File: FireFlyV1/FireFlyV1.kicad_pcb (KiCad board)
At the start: 2 copper layers, 2 parts, among them U1 RP2040, U2 W25Q32JVSS

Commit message: FireFlyV1 PCB begin
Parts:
- added C1: 15pF, Capacitor_SMD:C_0402_1005Metric, F.Cu at (149.2, 86.5)
- added C10: 0.1uF, Capacitor_SMD:C_0402_1005Metric, F.Cu at (152.1, 94.3)
- added C11: 1uF, Capacitor_SMD:C_0402_1005Metric, F.Cu at (155.0, 86.5)
- added C12: 1uF, Capacitor_SMD:C_0402_1005Metric, F.Cu at (155.0, 88.4)
- added C13: 100nF, Capacitor_SMD:C_0402_1005Metric, F.Cu at (155.0, 90.4)
- added C14: 100nF, Capacitor_SMD:C_0402_1005Metric, F.Cu at (155.0, 92.4)
- added C15: 100nF, Capacitor_SMD:C_0402_1005Metric, F.Cu at (155.0, 94.3)
- added C16: 100nF, Capacitor_SMD:C_0402_1005Metric, F.Cu at (157.9, 86.5)
- added C17: 100nF, Capacitor_SMD:C_0402_1005Metric, F.Cu at (157.9, 88.4)
- added C18: 100nF, Capacitor_SMD:C_0402_1005Metric, F.Cu at (157.9, 90.4)
- added C19: 100nF, Capacitor_SMD:C_0402_1005Metric, F.Cu at (157.9, 92.4)
- added C2: 15pF, Capacitor_SMD:C_0402_1005Metric, F.Cu at (149.2, 88.4)
- added C20: 1uF, Capacitor_SMD:C_0402_1005Metric, F.Cu at (157.9, 94.3)
- added C3: 10uF, Capacitor_SMD:C_0402_1005Metric, F.Cu at (149.2, 90.4)
- added C4: 10uF, Capacitor_SMD:C_0402_1005Metric, F.Cu at (149.2, 92.4)
- added C5: 10uF, Capacitor_SMD:C_0402_1005Metric, F.Cu at (149.2, 94.3)
- added C6: 2.2uF, Capacitor_SMD:C_0402_1005Metric, F.Cu at (152.1, 86.5)
- added C7: 33pF, Capacitor_SMD:C_0402_1005Metric, F.Cu at (152.1, 88.4)
- added C8: 10uF, Capacitor_SMD:C_0402_1005Metric, F.Cu at (152.1, 90.4)
- added C9: 0.1uF, Capacitor_SMD:C_0402_1005Metric, F.Cu at (152.1, 92.4)
- added J1: Conn_01x03, Connector_PinHeader_2.54mm:PinHeader_1x03_P2.54mm_Vertical, F.Cu at (126.1, 78.1)
- added J2: Conn_01x03, Connector_PinHeader_2.54mm:PinHeader_1x03_P2.54mm_Vertical, F.Cu at (130.8, 78.1)
- added J3: Conn_01x03, Connector_PinHeader_2.54mm:PinHeader_1x03_P2.54mm_Vertical, F.Cu at (135.4, 78.1)
- added J4: Conn_01x03, Connector_PinHeader_2.54mm:PinHeader_1x03_P2.54mm_Vertical, F.Cu at (140.1, 78.1)
- added J5: Conn_01x03, Connector_PinHeader_2.54mm:PinHeader_1x03_P2.54mm_Vertical, F.Cu at (144.7, 78.1)
- added LED1: KT-0603R, easyeda2kicad:LED0603-RD, F.Cu at (125.8, 86.8)
- added LED2: KT-0603R, easyeda2kicad:LED0603-RD, F.Cu at (125.8, 89.5)
- added LED3: KT-0603R, easyeda2kicad:LED0603-RD, F.Cu at (125.8, 92.1)
- added LED4: KT-0603R, easyeda2kicad:LED0603-RD, F.Cu at (125.8, 94.8)
- added LED5: KT-0603R, easyeda2kicad:LED0603-RD, F.Cu at (125.8, 97.4)
- added LED6: KT-0603R, easyeda2kicad:LED0603-RD, F.Cu at (125.8, 100.0)
- added LED7: KT-0603R, easyeda2kicad:LED0603-RD, F.Cu at (125.8, 102.7)
- added LED8: KT-0603R, easyeda2kicad:LED0603-RD, F.Cu at (125.8, 105.3)
- added LEDS1: ledstrip_3pin_10mm, mouser:ledstrip_3pin_10mm, F.Cu at (130.3, 86.2)
- added LEDS2: ledstrip_3pin_10mm, mouser:ledstrip_3pin_10mm, F.Cu at (135.3, 86.2)
- added LEDS3: ledstrip_3pin_10mm, mouser:ledstrip_3pin_10mm, F.Cu at (140.3, 86.2)
- added LEDS4: ledstrip_3pin_10mm, mouser:ledstrip_3pin_10mm, F.Cu at (145.3, 86.2)
- added MIC1: ZTS6216, easyeda2kicad:MIC-SMD_4P-L2.8-W1.9-P1.84-TL, F.Cu at (141.6, 121.5)
- added R1: 5.1K, Resistor_SMD:R_0402_1005Metric, F.Cu at (148.4, 113.6)
- added R10: 3.3k, Resistor_SMD:R_0402_1005Metric, F.Cu at (151.3, 117.6)
- added R11: 200k, Resistor_SMD:R_0402_1005Metric, F.Cu at (151.3, 119.6)
- added R12: 220, Resistor_SMD:R_0402_1005Metric, F.Cu at (151.3, 121.6)
- added R13: 220, Resistor_SMD:R_0402_1005Metric, F.Cu at (151.3, 123.6)
- added R14: 220, Resistor_SMD:R_0402_1005Metric, F.Cu at (151.3, 125.6)
- added R15: 100k, Resistor_SMD:R_0402_1005Metric, F.Cu at (154.2, 113.6)
- added R16: 0, Resistor_SMD:R_0402_1005Metric, F.Cu at (154.2, 115.6)
- added R17: 10k, Resistor_SMD:R_0402_1005Metric, F.Cu at (154.2, 117.6)
- added R18: 0, Resistor_SMD:R_0402_1005Metric, F.Cu at (154.2, 119.6)
- added R19: 220, Resistor_SMD:R_0402_1005Metric, F.Cu at (154.2, 121.6)
- added R2: 5.1K, Resistor_SMD:R_0402_1005Metric, F.Cu at (148.4, 115.6)
- added R20: 220, Resistor_SMD:R_0402_1005Metric, F.Cu at (154.2, 123.6)
- added R21: 220, Resistor_SMD:R_0402_1005Metric, F.Cu at (154.2, 125.6)
- added R22: 220, Resistor_SMD:R_0402_1005Metric, F.Cu at (157.1, 113.6)
- added R23: 220, Resistor_SMD:R_0402_1005Metric, F.Cu at (157.1, 115.6)
- added R24: 10k, Resistor_SMD:R_0402_1005Metric, F.Cu at (157.1, 117.6)
- added R25: 10k, Resistor_SMD:R_0402_1005Metric, F.Cu at (157.1, 119.6)
- added R3: 22, Resistor_SMD:R_0402_1005Metric, F.Cu at (148.4, 117.6)
- added R4: 22, Resistor_SMD:R_0402_1005Metric, F.Cu at (148.4, 119.6)
- added R5: 1K, Resistor_SMD:R_0402_1005Metric, F.Cu at (148.4, 121.6)
- added R6: 10K, Resistor_SMD:R_0402_1005Metric, F.Cu at (148.4, 123.6)
- added R7: 1K, Resistor_SMD:R_0402_1005Metric, F.Cu at (148.4, 125.6)
- added R8: 10K, Resistor_SMD:R_0402_1005Metric, F.Cu at (151.3, 113.6)
- added R9: 10K, Resistor_SMD:R_0402_1005Metric, F.Cu at (151.3, 115.6)
- added SW1: TS-1187A-B-A-B, easyeda2kicad:SW-SMD_4P-L5.1-W5.1-P3.70-LS6.5-TL-2, F.Cu at (163.2, 115.8)
- added SW2: TS-1187A-B-A-B, easyeda2kicad:SW-SMD_4P-L5.1-W5.1-P3.70-LS6.5-TL-2, F.Cu at (163.2, 122.2)
- added TP1: TestPoint, TestPoint:TestPoint_Loop_D1.80mm_Drill1.0mm_Beaded, F.Cu at (169.1, 78.1)
- added TP2: TestPoint, TestPoint:TestPoint_Loop_D1.80mm_Drill1.0mm_Beaded, F.Cu at (169.1, 82.8)
- added U3: AMS1117-3.3, easyeda2kicad:SOT-223-3_L6.5-W3.4-P2.30-LS7.0-BR, F.Cu at (162.0, 79.7)
- added U5: MCP6001T-I/OT, easyeda2kicad:SOT-23-5_L3.0-W1.7-P0.95-LS2.8-BR, F.Cu at (141.8, 116.9)
- added U6: 74HC595D,118, easyeda2kicad:SOIC-16_L9.9-W3.9-P1.27-LS6.0-BL, F.Cu at (133.8, 119.1)
- added U7: PEC12R-4215F-S0024, mouser:PEC12R-4XXXF-SXXXX_court, F.Cu at (137.4, 105.3)
- added USB1: USB-TYPE-C-018, easyeda2kicad:USB-C_SMD-TYPE-C-31-M-12, F.Cu at (164.7, 89.1)
- added VR1: PTV09A-4020F-B104, mouser:PTV09A4020FB103, F.Cu at (155.1, 104.2)
- added X1: X322512MSB4SI, easyeda2kicad:OSC-SMD_4P-L3.2-W2.5-BL, F.Cu at (166.1, 107.3)
- moved U1 20.4 mm to (167.9, 100.4)
- moved U2 11.8 mm to (152.2, 79.2)
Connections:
- U1 pad 1: Net-(U1-IOVDD-Pad1) -> 3V3
- U1 pad 10: Net-(U1-IOVDD-Pad1) -> 3V3
- U1 pad 13: unconnected-(U1-GPIO10-Pad13) -> SHIFT_DATA
- U1 pad 14: unconnected-(U1-GPIO11-Pad14) -> SHIFT_CLOCK
- U1 pad 15: unconnected-(U1-GPIO12-Pad15) -> SHIFT_LATCH
- U1 pad 17: unconnected-(U1-GPIO14-Pad17) -> LED_OUT_1
- U1 pad 18: unconnected-(U1-GPIO15-Pad18) -> LED_OUT_2
- U1 pad 19: unconnected-(U1-TESTEN-Pad19) -> BOARD_ID_0
- U1 pad 2: unconnected-(U1-GPIO0-Pad2) -> BOARD_ID_0
- U1 pad 20: unconnected-(U1-XIN-Pad20) -> XIN
- U1 pad 21: unconnected-(U1-XOUT-Pad21) -> XOUT
- U1 pad 22: Net-(U1-IOVDD-Pad1) -> 3V3
- U1 pad 23: Net-(U1-DVDD-Pad23) -> Net-(U1-VREG_VOUT)
- U1 pad 24: unconnected-(U1-SWCLK-Pad24) -> SWCLK
- U1 pad 25: unconnected-(U1-SWD-Pad25) -> SWDIO
- U1 pad 26: unconnected-(U1-RUN-Pad26) -> Net-(SW2-C)
- U1 pad 27: unconnected-(U1-GPIO16-Pad27) -> LED_OUT_3
- U1 pad 28: unconnected-(U1-GPIO17-Pad28) -> LED_OUT_4
- U1 pad 3: unconnected-(U1-GPIO1-Pad3) -> BOARD_ID_0
- U1 pad 33: Net-(U1-IOVDD-Pad1) -> 3V3
- U1 pad 34: unconnected-(U1-GPIO22-Pad34) -> BUTTON
- U1 pad 35: unconnected-(U1-GPIO23-Pad35) -> ENC_A
- U1 pad 36: unconnected-(U1-GPIO24-Pad36) -> ENC_B
- U1 pad 37: unconnected-(U1-GPIO25-Pad37) -> ENC_SW
- U1 pad 38: unconnected-(U1-GPIO26_ADC0-Pad38) -> MIC_ADC
- U1 pad 39: unconnected-(U1-GPIO27_ADC1-Pad39) -> POT_ADC
- U1 pad 4: unconnected-(U1-GPIO2-Pad4) -> BOARD_ID_0
- U1 pad 42: Net-(U1-IOVDD-Pad1) -> 3V3
- U1 pad 43: unconnected-(U1-ADC_AVDD-Pad43) -> 3V3
- U1 pad 44: unconnected-(U1-VREG_IN-Pad44) -> 3V3
- U1 pad 45: unconnected-(U1-VREG_VOUT-Pad45) -> Net-(U1-VREG_VOUT)
- U1 pad 46: unconnected-(U1-USB_DM-Pad46) -> Net-(U1-USB_DM)
- U1 pad 47: unconnected-(U1-USB_DP-Pad47) -> Net-(U1-USB_DP)
- U1 pad 48: unconnected-(U1-USB_VDD-Pad48) -> 3V3
- U1 pad 49: Net-(U1-IOVDD-Pad1) -> 3V3
- U1 pad 5: unconnected-(U1-GPIO3-Pad5) -> BOARD_ID_0
- U1 pad 50: Net-(U1-DVDD-Pad23) -> Net-(U1-VREG_VOUT)
- U1 pad 51: unconnected-(U1-QSPI_SD3-Pad51) -> QSPI_SD3
- U1 pad 52: unconnected-(U1-QSPI_SCLK-Pad52) -> QSPI_CLK
- U1 pad 53: unconnected-(U1-QSPI_SD0-Pad53) -> QSPI_SP0
- U1 pad 54: unconnected-(U1-QSPI_SD2-Pad54) -> QSPI_SD2
- U1 pad 55: unconnected-(U1-QSPI_SD1-Pad55) -> QSPI_SP1
- U1 pad 56: unconnected-(U1-QSPI_SS-Pad56) -> QSPI_SS
- U1 pad 57: GND -> BOARD_ID_0
- U1 pad 6: unconnected-(U1-GPIO4-Pad6) -> BOARD_ID_0
- U2 pad 1: unconnected-(U2-~{CS}-Pad1) -> QSPI_SS
- U2 pad 2: unconnected-(U2-DO(IO1)-Pad2) -> QSPI_SP1
- U2 pad 3: unconnected-(U2-IO2-Pad3) -> QSPI_SD2
- U2 pad 4: unconnected-(U2-GND-Pad4) -> BOARD_ID_0
- U2 pad 5: unconnected-(U2-DI(IO0)-Pad5) -> QSPI_SP0
- U2 pad 6: unconnected-(U2-CLK-Pad6) -> QSPI_CLK
- U2 pad 7: unconnected-(U2-IO3-Pad7) -> QSPI_SD3
- U2 pad 8: unconnected-(U2-VCC-Pad8) -> 3V3

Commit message: FireFlyV1 components layout initial thoughts
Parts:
- removed TP1, TP2: TestPoint, TestPoint:TestPoint_Loop_D1.80mm_Drill1.0mm_Beaded
- added J6: Conn_01x02_Pin, Connector_PinHeader_2.54mm:PinHeader_1x02_P2.54mm_Vertical, F.Cu at (188.1, 114.4)
- LEDS1, LEDS2, LEDS3, LEDS4, U7, VR1: moved to B.Cu
- moved LED5 122.7 mm to (248.5, 95.5), turned to 60 degrees
- moved LED4 121.2 mm to (247.0, 98.5)
- moved LED3 117.8 mm to (243.5, 97.5)
- moved LED7 117.1 mm to (242.7, 94.5)
- moved LED8 117.0 mm to (242.0, 91.5), turned to 180 degrees
- moved LED1 116.8 mm to (242.0, 99.0), turned to 180 degrees
- moved J1 116.2 mm to (238.5, 107.5), turned to 30 degrees
- moved LED6 112.9 mm to (238.6, 95.3), turned to -60 degrees
- moved LED2 110.6 mm to (236.4, 90.7), turned to -60 degrees
- moved R20 97.9 mm to (248.0, 95.5)
- moved U6 96.1 mm to (227.7, 98.5), turned to 180 degrees
- moved R7 96.1 mm to (244.0, 116.5)
- moved R14 95.2 mm to (242.3, 97.5)
- moved R19 95.1 mm to (246.5, 98.5)
- moved R12 94.7 mm to (243.3, 99.0)
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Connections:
- R6 pad 1: unconnected-(R6-Pad1) -> 3V3
- SW2 pad 1: BOARD_ID_0 -> unconnected-(SW2-A-Pad1)
- SW2 pad 2: unconnected-(SW2-B-Pad2) -> BOARD_ID_0
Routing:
- net XIN: track 0.00 -> 5.77 mm
- net BOARD_ID_0: track 0.00 -> 3.84 mm
- net XOUT: track 0.00 -> 3.69 mm
- net Net-(X1-OSC2): track 0.00 -> 2.83 mm
- added copper zone on F.Cu, net BOARD_ID_0
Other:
- board outline added: 269.5 x 119.7 mm
- board text added: "Just power"
- board text added: "shapes are for assisting positioning only for now"

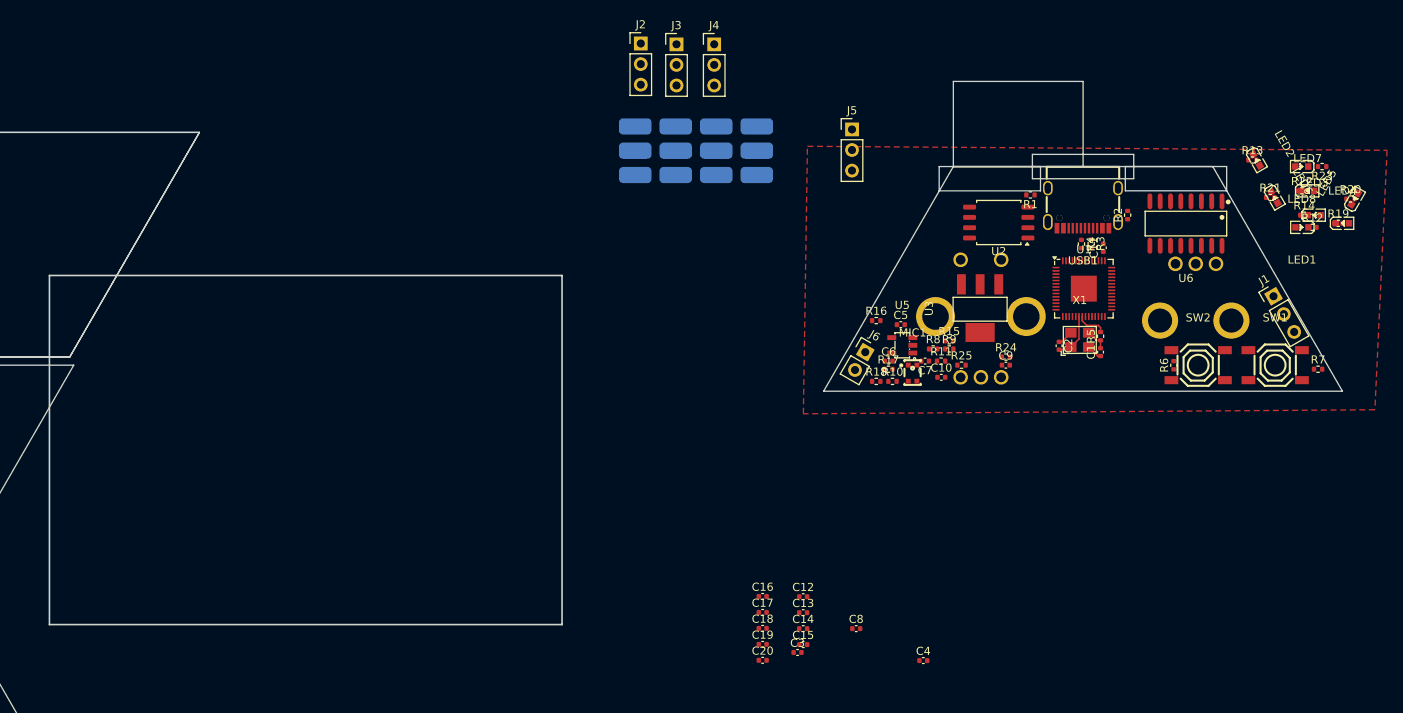
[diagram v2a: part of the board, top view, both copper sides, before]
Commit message: FireFlyV1 mostly fit on the board
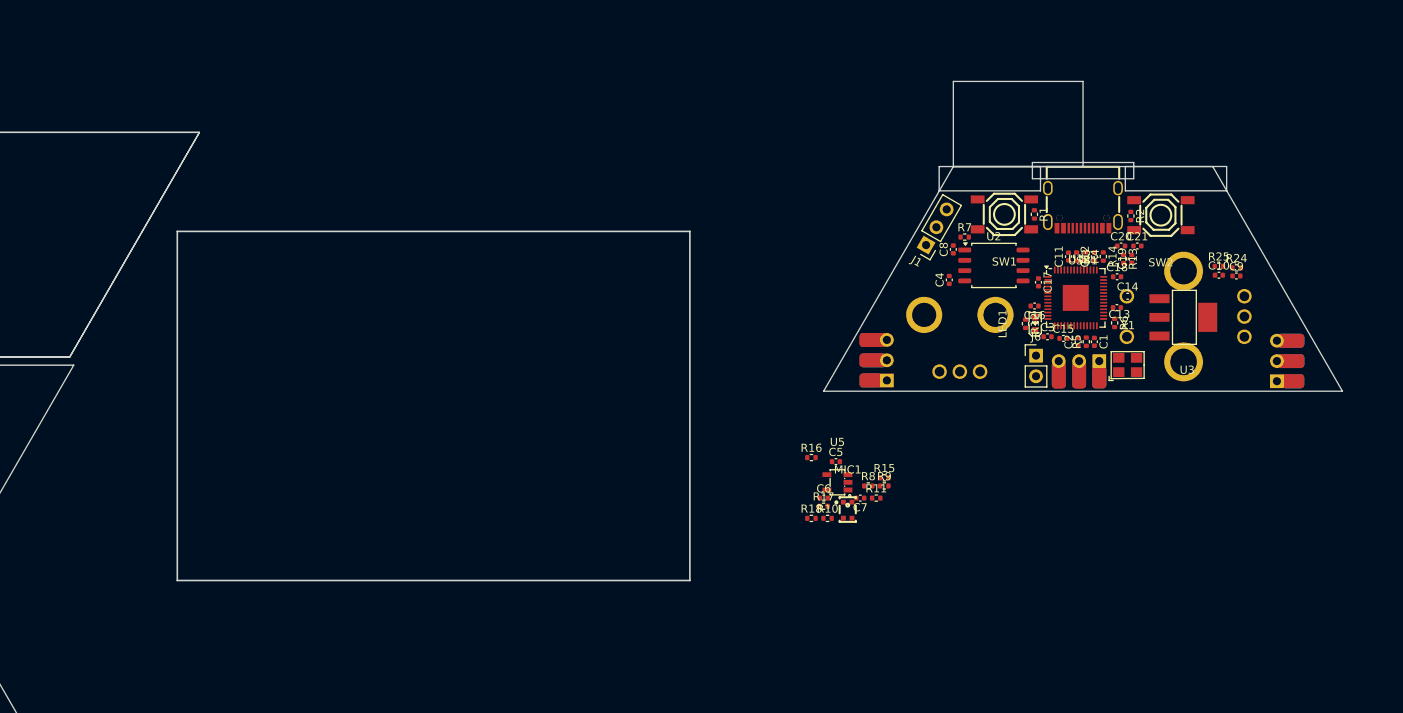
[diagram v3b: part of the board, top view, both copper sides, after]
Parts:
- removed J2, J3, J4, J5: Conn_01x03, Connector_PinHeader_2.54mm:PinHeader_1x03_P2.54mm_Vertical
- removed LED2, LED3, LED4, LED5, LED6, LED7, LED8: KT-0603R, easyeda2kicad:LED0603-RD
- removed LEDS4: ledstrip_3pin_10mm, mouser:ledstrip_3pin_10mm
- removed R19, R20, R21, R22, R23: 220, Resistor_SMD:R_0402_1005Metric
- removed U6: 74HC595D,118, easyeda2kicad:SOIC-16_L9.9-W3.9-P1.27-LS6.0-BL
- added C21: 100nF, Capacitor_SMD:C_0402_1005Metric, F.Cu at (221.7, 101.3)
- C19: value 100nF -> 2.2uF
- C20: value 1uF -> 100nF
- LEDS1, LEDS2: footprint mouser:ledstrip_3pin_10mm -> mouser:ledstrip_3pin_withpins
- LEDS3: footprint mouser:ledstrip_3pin_10mm -> mouser:ledstrip_3pin_withpins; moved to F.Cu
- R14: value 220 -> 0
- moved LEDS3 83.6 mm to (242.4, 115.5)
- moved C20 67.6 mm to (219.7, 101.3)
- moved C19 65.8 mm to (221.0, 102.9), turned to 90 degrees
- moved C18 61.6 mm to (219.2, 105.1)
- moved C14 57.3 mm to (220.5, 107.5)
- moved LEDS2 56.5 mm to (214.5, 119.0), turned to 90 degrees
- moved C12 55.2 mm to (216.4, 102.6), turned to 90 degrees
- moved C13 54.0 mm to (219.2, 108.9)
- moved C17 53.1 mm to (209.5, 105.8), turned to -90 degrees
- moved C3 49.7 mm to (210.6, 112.5)
- moved C15 49.6 mm to (212.6, 112.7)
- moved C16 49.1 mm to (209.0, 108.7), turned to 180 degrees
- moved C8 48.3 mm to (199.0, 101.7), turned to 90 degrees
- moved C4 47.1 mm to (198.5, 105.5), turned to 90 degrees
- moved R7 46.5 mm to (200.4, 100.2)
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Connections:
- C19 pad 1: 3V3 -> ADC_VREF
- C20 pad 1: 3V3 -> Net-(U1-VREG_VOUT)
- LED1 pad 2: SHIFT_Q0 -> STATUS_LED
- R13 pad 1: BOARD_ID_0 -> 3V3
- R13 pad 2: Net-(LED2-K) -> ADC_VREF
- R14 pad 1: BOARD_ID_0 -> 3V3
- R14 pad 2: Net-(LED3-K) -> ADC_VREF
- R6 pad 2: Net-(SW2-C) -> Net-(SW2-D)
- SW2 pad 1: unconnected-(SW2-A-Pad1) -> BOARD_ID_0
- SW2 pad 3: Net-(SW2-C) -> unconnected-(SW2-C-Pad3)
- SW2 pad 4: unconnected-(SW2-D-Pad4) -> Net-(SW2-D)
- U1 pad 13: SHIFT_DATA -> STATUS_LED
- U1 pad 14: SHIFT_CLOCK -> unconnected-(U1-GPIO11-Pad14)
- U1 pad 15: SHIFT_LATCH -> unconnected-(U1-GPIO12-Pad15)
- U1 pad 26: Net-(SW2-C) -> Net-(SW2-D)
- U1 pad 28: LED_OUT_4 -> unconnected-(U1-GPIO17-Pad28)
- U1 pad 43: 3V3 -> ADC_VREF
- USB1 pad 1: (no net) -> BOARD_ID_0
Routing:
- net XIN: track 5.77 -> 0.00 mm
- net BOARD_ID_0: track 3.84 -> 0.00 mm
- net XOUT: track 3.69 -> 0.00 mm
- net Net-(X1-OSC2): track 2.83 -> 0.00 mm
- removed copper zone on F.Cu, net BOARD_ID_0
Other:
- outline, holes or cut-outs redrawn
- board text added: "mic stuff"
- board text removed: "Just power"

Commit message: FireFlyV1 everything on board
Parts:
- removed J6: Conn_01x02_Pin, Connector_PinHeader_2.54mm:PinHeader_1x02_P2.54mm_Vertical
- added J2: Conn_01x01_Pin, Connector_PinHeader_2.54mm:PinHeader_1x01_P2.54mm_Vertical, F.Cu at (194.1, 105.3)
- added J3: Conn_01x01_Pin, Connector_PinHeader_2.54mm:PinHeader_1x01_P2.54mm_Vertical, F.Cu at (209.0, 115.0)
- C5: value 10uF -> 1uF
- moved MIC1 28.9 mm to (200.4, 108.8), turned to 180 degrees
- moved R8 27.9 mm to (197.4, 104.5), turned to 90 degrees
- moved R10 27.8 mm to (198.4, 111.4), turned to 90 degrees
- moved C6 27.7 mm to (198.4, 109.4), turned to -90 degrees
- moved C4 26.9 mm to (223.8, 114.6), turned to -90 degrees
- moved R9 25.3 mm to (197.4, 106.6), turned to 90 degrees
- moved R18 25.1 mm to (195.8, 114.3)
- moved R16 24.8 mm to (204.5, 118.1)
- moved R11 24.5 mm to (205.5, 113.9)
- moved R17 24.4 mm to (196.6, 113.1)
- moved C5 24.0 mm to (203.1, 112.7), turned to 180 degrees
- moved C7 23.4 mm to (203.0, 114.9)
- moved U5 22.5 mm to (199.9, 113.9)
- moved R15 19.3 mm to (204.7, 116.8)
- moved X1 0.14 mm to (220.6, 115.9)
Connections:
- R18 pad 1: unconnected-(R18-Pad1) -> Net-(U5-VIN-)
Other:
- board text removed: "mic stuff"
